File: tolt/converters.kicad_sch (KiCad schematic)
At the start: 54 parts, among them J11 Conn_01x05, U14 AMS1117-3.3, U15 LP5907MFX-3.3, U16 TPS62173DSG, U19 TLV61047DDC, U24 LTC7138xMSE

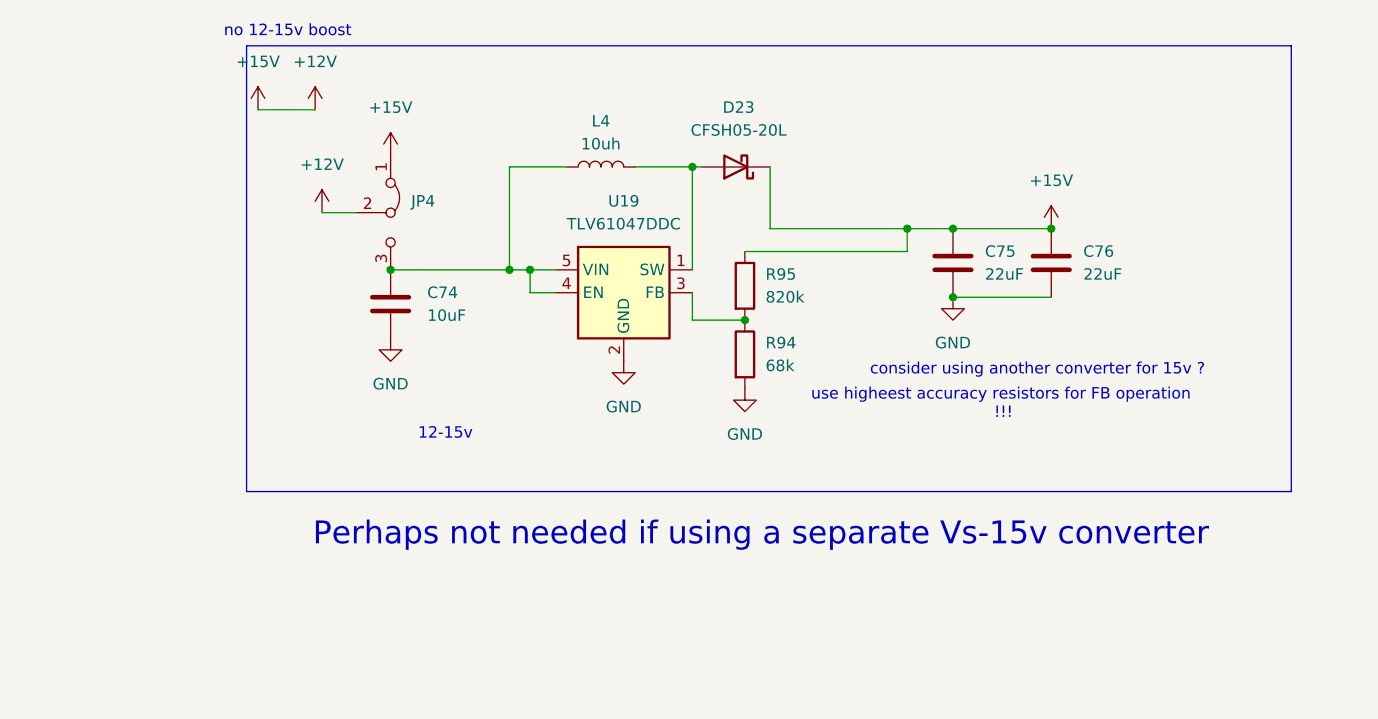
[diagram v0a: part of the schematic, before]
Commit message: big update
fixed decoupling correctly
more gnd plane work and routing finished
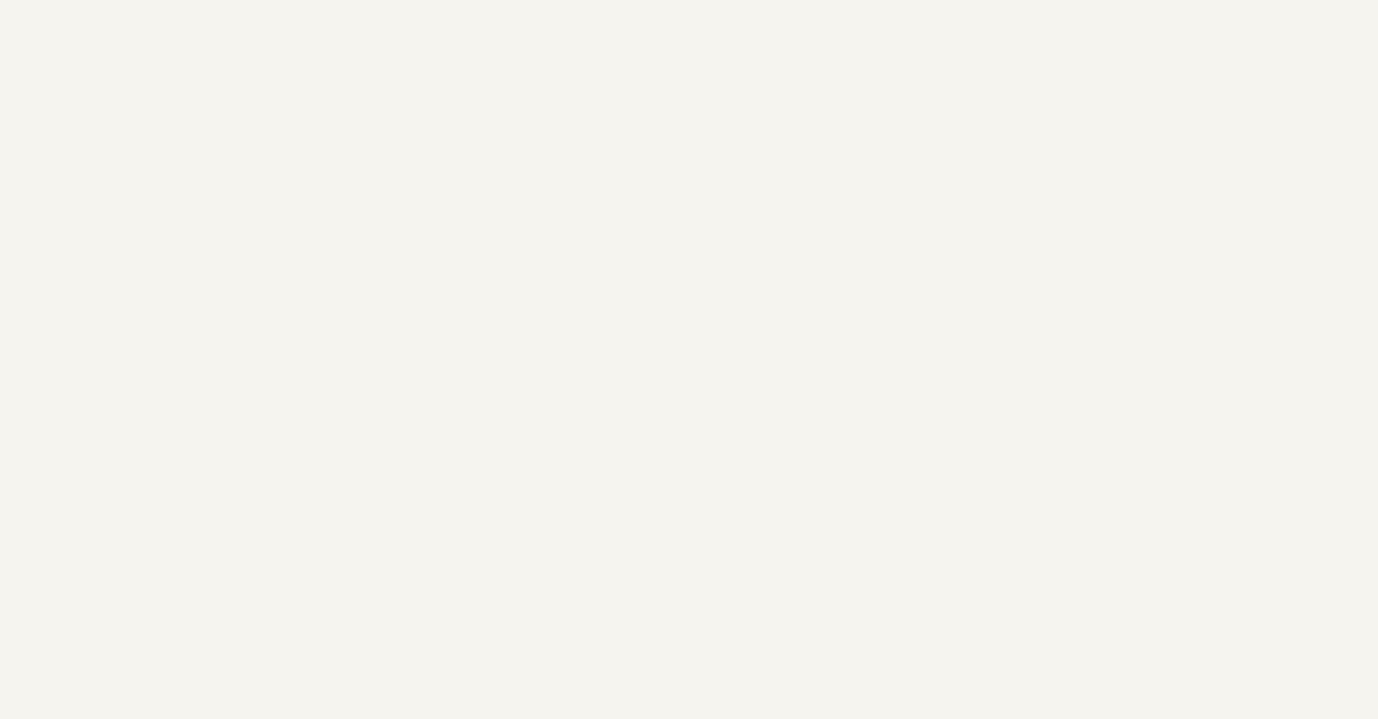
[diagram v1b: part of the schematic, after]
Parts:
- removed C74: 10uF, Capacitor_SMD:C_1210_3225Metric, symbol Device:C
- removed C75, C76: 22uF, Capacitor_SMD:C_1210_3225Metric, symbol Device:C
- removed D23: CFSH05-20L, Diode_SMD:D_SOD-882, symbol Device:D_Schottky
- removed JP4: Jumper_3_Bridged12, Jumper:SolderJumper-3_P1.3mm_Bridged2Bar12_RoundedPad1.0x1.5mm, symbol Jumper:Jumper_3_Bridged12
- removed L4: 10uh, Inductor_SMD:L_Abracon_ASPI-4030S, symbol Device:L
- removed R94: 68k, Resistor_SMD:R_0603_1608Metric, symbol Device:R
- removed R95: 820k, Resistor_SMD:R_0603_1608Metric, symbol Device:R
- removed U19: TLV61047DDC, Package_TO_SOT_SMD:SOT-23-5, symbol Regulator_Switching:TLV61047DDC
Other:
- note removed: "12-15v"
- note removed: "Perhaps not needed if using a separate Vs-15v converter"
- note removed: "consider using another converter for 15v ?"
- note removed: "no 12-15v boost"
- note removed: "use higheest accuracy resistors for FB operation !!!"

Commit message: 12v
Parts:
- added C147: 100n, Capacitor_SMD:C_1210_3225Metric, symbol Device:C
- added C150: 100nF, Capacitor_SMD:C_1206_3216Metric_Pad1.33x1.80mm_HandSolder, symbol Device:C
- added C151: 10uF, Capacitor_Tantalum_SMD:CP_EIA-3216-18_Kemet-A, symbol Device:C
- added C152: 100uF, Capacitor_SMD:CP_Elec_6.3x5.4, symbol Device:C
- added C74: 33uF, Capacitor_THT:CP_Radial_D10.0mm_P2.50mm_P5.00mm, symbol Device:C
- added C75: 470nF, Capacitor_SMD:C_1210_3225Metric, symbol Device:C
- added D33, D34: STTH1R06U, Diode_SMD:D_SMB, symbol Device:D
- added JP6: Jumper_2_Open, Connector_PinHeader_2.54mm:PinHeader_1x02_P2.54mm_Vertical, symbol Jumper:Jumper_2_Open
- added L4: 1.5mH, Inductor_SMD:L_Bourns_SRN8040TA, symbol Device:L
- added R117: 2k, Resistor_SMD:R_2512_6332Metric, symbol Device:R
- added R118: 12.7k, Resistor_SMD:R_1206_3216Metric, symbol Device:R
- added R119: 0, Resistor_SMD:R_0603_1608Metric, symbol Device:R
- added R120: 4k, Resistor_SMD:R_0603_1608Metric, symbol Device:R
- added U25: LNK306D, EasyEDA2KiCad:SO-8C_7P-L4.9-W3.9-P1.27-LS6.0-BL-PE3, symbol Regulator_Switching:LNK306D
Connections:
- net +12V: now also C152.1, D34.2 (A), L4.2, R120.1
- net +BATT: now also C147.1, JP6.1 (A)
- net GND: now also C152.2, C74.2, C75.2, D33.2 (A), R120.2
- new net: R117.1, R118.1, U25.2 (FB)
- new net: C151.1, D34.1 (K), R118.2
- new net: C147.2, JP6.2 (B), R119.1
- new net: C74.1, C75.1, R119.2, U25.4 (D)
- new net: C150.2, C151.2, D33.1 (K), L4.1, R117.2, U25.5 (S), U25.6 (S), U25.7 (S), U25.8 (S)
- new net: C150.1, U25.1 (BP)
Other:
- note added: "need to fiddle with Feedback for stable 12v"
- note added: "needs to be 200v+ cap"

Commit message: extra buck added
placed and routed
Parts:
- U25: footprint EasyEDA2KiCad:SO-8C_7P-L4.9-W3.9-P1.27-LS6.0-BL-PE3 -> Package_SO:PowerIntegrations_SO-8C
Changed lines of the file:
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@@
 			)
 		)
-		(property "Footprint" "EasyEDA2KiCad:SO-8C_7P-L4.9-W3.9-P1.27-LS6.0-BL-PE3"
+		(property "Footprint" "Package_SO:PowerIntegrations_SO-8C"
 			(at 250.444 54.356 0)
 			(effects
@@
 		)
 		(property "Datasheet" "http://www.powerint.com/sites/default/files/product-docs/lnk302_304-306.pdf"
-			(at 250.444 54.356 0)
+			(at 245.364 66.802 0)
 			(effects
 				(font

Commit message: 12vdc
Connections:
- net +BATT: no longer C147.1
- net GND: now also C147.2
- net at JP6.2 (B), R119.1: no longer C147.2
- net at C74.1, C75.1, R119.2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: now also C147.1
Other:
- moved on the sheet: C147, JP6
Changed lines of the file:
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@@
 	)
 	(junction
-		(at 200.152 42.418)
+		(at 157.48 96.52)
 		(diameter 0)
 		(color 0 0 0 0)
 	)
 	(junction
-		(at 157.48 96.52)
+		(at 63.754 106.426)
 		(diameter 0)
 		(color 0 0 0 0)
 	)
 	(junction
-		(at 63.754 106.426)
+		(at 315.722 54.356)
 		(diameter 0)
 		(color 0 0 0 0)
 	)
 	(junction
-		(at 315.722 54.356)
+		(at 215.392 54.356)
 		(diameter 0)
 		(color 0 0 0 0)
@@
 	)
 	(junction
+		(at 219.964 61.976)
+		(diameter 0)
+		(color 0 0 0 0)
+	)
+	(junction
 		(at 338.328 199.644)
 		(diameter 0)
@@
 	)
 	(junction
-		(at 211.582 54.356)
-		(diameter 0)
-		(color 0 0 0 0)
-	)
-	(junction
 		(at 112.268 48.514)
 		(diameter 0)
@@
 	(wire
 		(pts
-			(xy 200.152 42.418) (xy 200.152 54.356)
-		)
-		(stroke
-			(width 0)
-			(type default)
-		)
-	)
-	(wire
-		(pts
 			(xy 169.926 96.52) (xy 179.07 96.52)
 		)
@@
 	(wire
 		(pts
-			(xy 211.582 54.356) (xy 212.598 54.356)
-		)
-		(stroke
-			(width 0)
-			(type default)
-		)
-	)
-	(wire
-		(pts
 			(xy 60.96 163.576) (xy 60.96 181.61)
 		)
@@
 	(wire
 		(pts
-			(xy 211.582 54.356) (xy 209.296 54.356)
-		)
-		(stroke
-			(width 0)
-			(type default)
-		)
-	)
-	(wire
-		(pts
-			(xy 200.152 54.356) (xy 199.136 54.356)
+			(xy 200.914 54.356) (xy 204.216 54.356)
 		)
 		(stroke
@@
 	(wire
 		(pts
-			(xy 220.218 54.356) (xy 222.758 54.356)
+			(xy 286.004 52.832) (xy 286.004 54.356)
 		)
 		(stroke
@@
 	(wire
 		(pts
-			(xy 286.004 52.832) (xy 286.004 54.356)
+			(xy 211.836 54.356) (xy 215.392 54.356)
 		)
 		(stroke
@@
 	(wire
 		(pts
-			(xy 198.882 42.418) (xy 200.152 42.418)
-		)
-		(stroke
-			(width 0)
-			(type default)
-		)
-	)
-	(wire
-		(pts
 			(xy 275.844 54.356) (xy 264.922 54.356)
 		)
@@
 	(wire
 		(pts
+			(xy 215.392 61.976) (xy 219.964 61.976)
+		)
+		(stroke
+			(width 0)
+			(type default)
+		)
+	)
+	(wire
+		(pts
 			(xy 160.274 161.036) (xy 148.844 161.036)
 		)
@@
 	(wire
 		(pts
-			(xy 207.772 42.418) (xy 211.582 42.418)
+			(xy 215.392 54.356) (xy 222.758 54.356)
 		)
 		(stroke
@@
 	(wire
 		(pts
-			(xy 211.582 42.418) (xy 211.582 54.356)
+			(xy 184.912 54.356) (xy 190.754 54.356)
 		)
 		(stroke
@@
 	(symbol
 		(lib_id "Device:R")
-		(at 216.408 54.356 90)
+		(at 208.026 54.356 90)
 		(unit 1)
 		(exclude_from_sim no)
@@
 		(on_board yes)
 		(dnp yes)
-		(fields_autoplaced yes)
 		(property "Reference" "R119"
-			(at 216.408 48.006 90)
+			(at 194.31 45.974 90)
 			(effects
 				(font
 					(size 1.27 1.27)
 				)
+				(hide yes)
 			)
 		)
 		(property "Value" "0"
-			(at 216.408 50.546 90)
+			(at 208.026 50.546 90)
 			(effects
 				(font
@@
 		)
 		(property "Footprint" "Resistor_SMD:R_0603_1608Metric"
-			(at 216.408 56.134 90)
+			(at 208.026 56.134 90)
 			(effects
 				(font
@@
 		)
 		(property "Datasheet" "~"
-			(at 216.408 54.356 0)
+			(at 208.026 54.356 0)
 			(effects
 				(font
@@
 		)
 		(property "Description" "Resistor"
-			(at 216.408 54.356 0)
+			(at 208.026 54.356 0)
 			(effects
 				(font
@@
 		)
 		(property "Availability" ""
-			(at 216.408 54.356 0)
+			(at 208.026 54.356 0)
 			(effects
 				(font
@@
 		)
 		(property "Check_prices" ""
-			(at 216.408 54.356 0)
+			(at 208.026 54.356 0)
 			(effects
 				(font
@@
 		)
 		(property "Description_1" ""
-			(at 216.408 54.356 0)
+			(at 208.026 54.356 0)
 			(effects
 				(font
@@
 		)
 		(property "MANUFACTURER" ""
-			(at 216.408 54.356 0)
+			(at 208.026 54.356 0)
 			(effects
 				(font
@@
 		)
 		(property "MAXIMUM_PACKAGE_HEIGHT" ""
-			(at 216.408 54.356 0)
+			(at 208.026 54.356 0)
 			(effects
 				(font
@@
 		)
 		(property "MF" ""
-			(at 216.408 54.356 0)
+			(at 208.026 54.356 0)
 			(effects
 				(font
@@
 		)
 		(property "MFR PT" ""
-			(at 216.408 54.356 0)
+			(at 208.026 54.356 0)
 			(effects
 				(font
@@
 		)
 		(property "MP" ""
-			(at 216.408 54.356 0)
+			(at 208.026 54.356 0)
 			(effects
 				(font
@@
 		)
 		(property "PARTREV" ""
-			(at 216.408 54.356 0)
+			(at 208.026 54.356 0)
 			(effects
 				(font
@@
 		)
 		(property "Package" ""
-			(at 216.408 54.356 0)
+			(at 208.026 54.356 0)
 			(effects
 				(font
@@
 		)
 		(property "Price" ""
-			(at 216.408 54.356 0)
+			(at 208.026 54.356 0)
 			(effects
 				(font
@@
 		)
 		(property "STANDARD" ""
-			(at 216.408 54.356 0)
+			(at 208.026 54.356 0)
 			(effects
 				(font
@@
 		)
 		(property "SnapEDA_Link" ""
-			(at 216.408 54.356 0)
+			(at 208.026 54.356 0)
 			(effects
 				(font
@@
 	(symbol
 		(lib_id "power:+BATT")
-		(at 198.882 42.418 0)
+		(at 184.912 54.356 0)
 		(unit 1)
 		(exclude_from_sim no)
@@
 		(fields_autoplaced yes)
 		(property "Reference" "#PWR0164"
-			(at 198.882 46.228 0)
+			(at 184.912 58.166 0)
 			(effects
 				(font
@@
 		)
 		(property "Value" "+BATT"
-			(at 198.882 37.338 0)
+			(at 184.912 49.276 0)
 			(effects
 				(font
@@
 		)
 		(property "Footprint" ""
-			(at 198.882 42.418 0)
+			(at 184.912 54.356 0)
 			(effects
 				(font
@@
 		)
 		(property "Datasheet" ""
-			(at 198.882 42.418 0)
+			(at 184.912 54.356 0)
 			(effects
 				(font
@@
 		)
 		(property "Description" "Power symbol creates a global label with name \"+BATT\""
-			(at 198.882 42.418 0)
+			(at 184.912 54.356 0)
 			(effects
 				(font
@@
 	(symbol
 		(lib_id "Device:C")
-		(at 203.962 42.418 90)
+		(at 215.392 58.166 0)
 		(unit 1)
 		(exclude_from_sim no)
@@
 		(fields_autoplaced yes)
 		(property "Reference" "C147"
-			(at 203.962 34.798 90)
+			(at 218.44 56.8959 0)
 			(effects
 				(font
 					(size 1.27 1.27)
 				)
+				(justify left)
 			)
 		)
 		(property "Value" "100n"
-			(at 203.962 37.338 90)
+			(at 218.44 59.4359 0)
 			(effects
 				(font
 					(size 1.27 1.27)
 				)
+				(justify left)
 			)
 		)
 		(property "Footprint" "Capacitor_SMD:C_1210_3225Metric"
-			(at 207.772 41.4528 0)
+			(at 216.3572 61.976 0)
 			(effects
 				(font
@@
 		)
 		(property "Datasheet" "~"
-			(at 203.962 42.418 0)
+			(at 215.392 58.166 0)
 			(effects
 				(font
@@
 		)
 		(property "Description" "Unpolarized capacitor"
-			(at 203.962 42.418 0)
+			(at 215.392 58.166 0)
 			(effects
 				(font
@@
 	(symbol
 		(lib_id "Jumper:Jumper_2_Open")
-		(at 204.216 54.356 0)
+		(at 195.834 54.356 0)
 		(unit 1)
 		(exclude_from_sim yes)
@@
 		(on_board yes)
 		(dnp no)
-		(fields_autoplaced yes)
 		(property "Reference" "JP6"
-			(at 204.216 47.498 0)
+			(at 195.834 57.658 0)
 			(effects
 				(font
@@
 		)
 		(property "Value" "Jumper_2_Open"
-			(at 204.216 50.038 0)
+			(at 195.834 50.038 0)
 			(effects
 				(font
@@
 		)
 		(property "Footprint" "Connector_PinHeader_2.54mm:PinHeader_1x02_P2.54mm_Vertical"
-			(at 204.216 54.356 0)
+			(at 195.834 54.356 0)
 			(effects
 				(font
@@
 		)
 		(property "Datasheet" "~"
-			(at 204.216 54.356 0)
+			(at 195.834 54.356 0)
 			(effects
 				(font
@@
 		)
 		(property "Description" "Jumper, 2-pole, open"
-			(at 204.216 54.356 0)
+			(at 195.834 54.356 0)
 			(effects
 				(font

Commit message: begenning of lcsc part assign
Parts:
- C102, C105: footprint Capacitor_SMD:C_2220_5750Metric_Pad1.97x5.40mm_HandSolder -> Capacitor_SMD:C_2220_5750Metric
- C149, C71, C73, C85: LCSC (none) -> C138687
- C150: footprint Capacitor_SMD:C_1206_3216Metric_Pad1.33x1.80mm_HandSolder -> Capacitor_SMD:C_1206_3216Metric
- C66: LCSC (none) -> C15008
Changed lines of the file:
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@@
 			)
 		)
+		(property "LCSC" "C138687"
+			(at 170.942 164.846 0)
+			(effects
+				(font
+					(size 1.27 1.27)
+				)
+				(hide yes)
+			)
+		)
 		(pin "1"
 		)
@@
 			)
 		)
+		(property "LCSC" "C138687"
+			(at 112.268 44.704 0)
+			(effects
+				(font
+					(size 1.27 1.27)
+				)
+				(hide yes)
+			)
+		)
 		(pin "1"
 		)
@@
 			)
 		)
+		(property "LCSC" "C138687"
+			(at 148.844 164.846 0)
+			(effects
+				(font
+					(size 1.27 1.27)
+				)
+				(hide yes)
+			)
+		)
 		(pin "1"
 		)
@@
 			)
 		)
+		(property "LCSC" "C138687"
+			(at 47.752 43.688 0)
+			(effects
+				(font
+					(size 1.27 1.27)
+				)
+				(hide yes)
+			)
+		)
 		(pin "1"
 		)
@@
 			)
 		)
-		(property "Footprint" "Capacitor_SMD:C_2220_5750Metric_Pad1.97x5.40mm_HandSolder"
+		(property "Footprint" "Capacitor_SMD:C_2220_5750Metric"
 			(at 20.0152 177.8 0)
 			(effects
@@
 			)
 		)
-		(property "Footprint" "Capacitor_SMD:C_2220_5750Metric_Pad1.97x5.40mm_HandSolder"
+		(property "Footprint" "Capacitor_SMD:C_2220_5750Metric"
 			(at 31.4452 177.8 0)
 			(effects
@@
 			)
 		)
-		(property "Footprint" "Capacitor_SMD:C_1206_3216Metric_Pad1.33x1.80mm_HandSolder"
+		(property "Footprint" "Capacitor_SMD:C_1206_3216Metric"
 			(at 265.8872 54.356 0)
 			(effects
@@
 			(at 222.758 100.33 0)
 			(effects
+				(font
+					(size 1.27 1.27)
+				)
+				(hide yes)
+			)
+		)
+		(property "LCSC" "C15008"
+			(at 222.758 100.33 0)
+			(effects

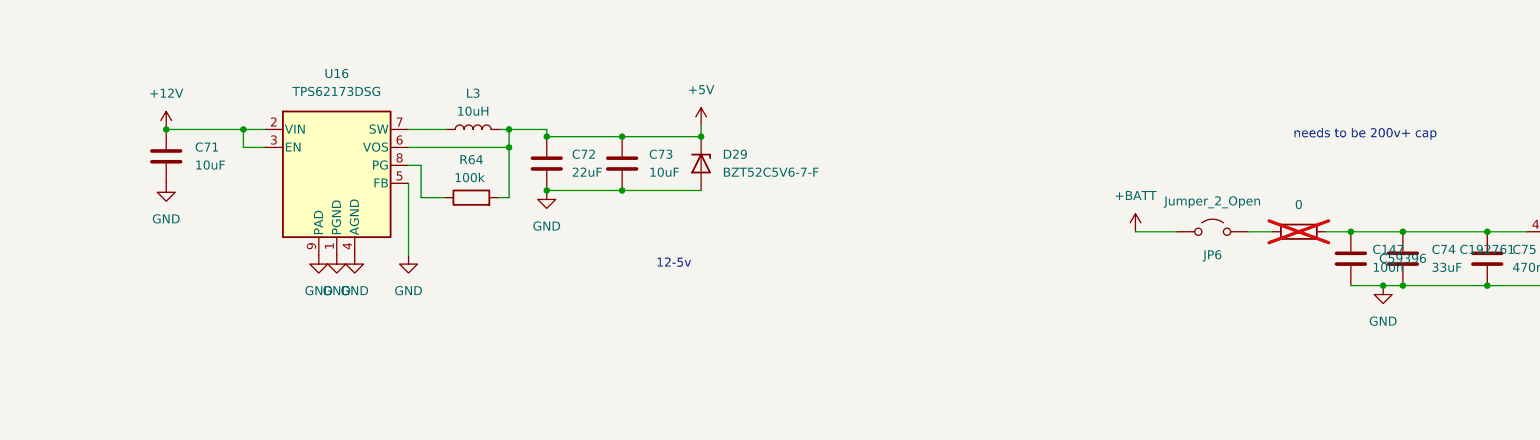
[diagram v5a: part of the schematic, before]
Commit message: more assign+12-5v change
changed with TPS82130
Since using esp32 will increase consumption by a lot
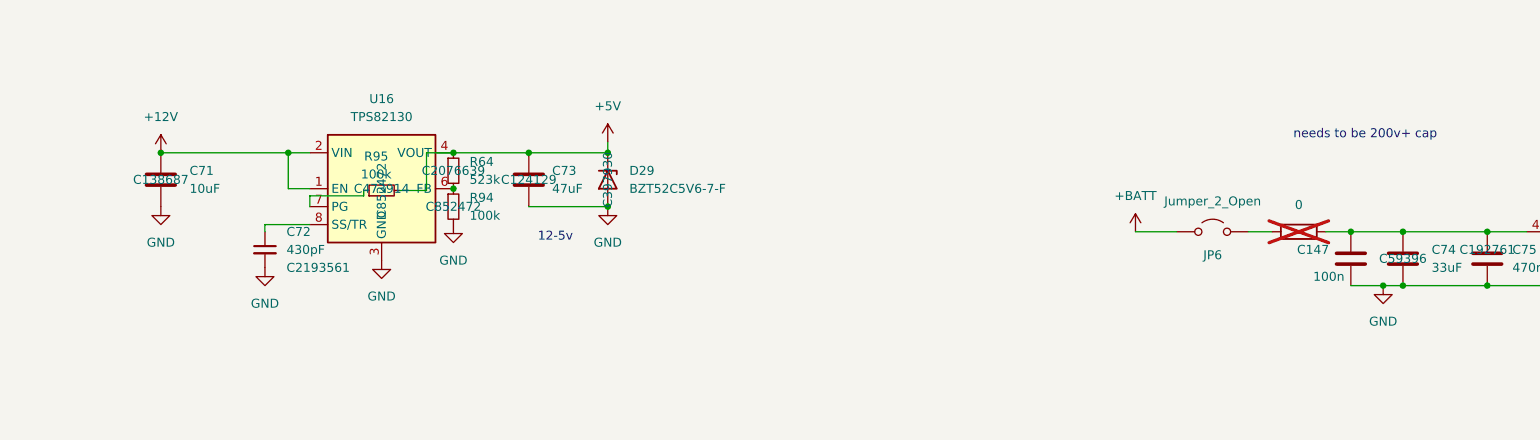
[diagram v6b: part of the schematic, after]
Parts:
- removed C72: 22uF, Capacitor_SMD:C_1210_3225Metric, symbol Device:C
- removed L3: 10uH, Library:IND-SMD_L5.0-W5.0, symbol Device:L
- removed R64: 100k, Resistor_SMD:R_0603_1608Metric, symbol Device:R
- removed U16: TPS62173DSG, Package_SON:WSON-8-1EP_2x2mm_P0.5mm_EP0.9x1.6mm, symbol Regulator_Switching:TPS62173DSG
- added C72: 430pF, Resistor_SMD:R_0402_1005Metric, symbol Device:C_Small
- added R64: 523k, Resistor_SMD:R_0402_1005Metric, symbol Device:R_Small
- added R94, R95: 100k, Resistor_SMD:R_0402_1005Metric, symbol Device:R_Small
- added U16: TPS82130, Package_LGA:Texas_SIL0008D_MicroSiP-8-1EP_2.8x3mm_P0.65mm_EP1.1x1.9mm_ThermalVias, symbol Regulator_Switching:TPS82130
- C73: value 10uF -> 47uF; footprint Capacitor_SMD:C_1210_3225Metric -> Capacitor_SMD:C_0805_2012Metric; LCSC C138687 -> C124129
- D29: LCSC (none) -> C397930
- R4, R68, R69: LCSC (none) -> C149816
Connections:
- net +12V: now also U16.1 (EN), U16.2 (VIN)
- net +5V: now also R64.1, R95.2, U16.4 (VOUT), U16.5 (VOUT)
- net GND: now also C72.2, R94.2, U16.3 (GND), U16.9 (GND)
- new net: C72.1, U16.8 (SS/TR)
- new net: R64.2, R94.1, U16.6 (FB)
- new net: R95.1, U16.7 (PG)
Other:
- moved on the sheet: C71, C73, D29
